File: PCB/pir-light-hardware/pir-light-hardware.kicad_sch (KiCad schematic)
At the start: 3 parts

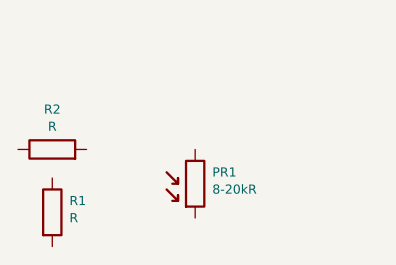
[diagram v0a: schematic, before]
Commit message: chore(kicad): add next part of component libraries
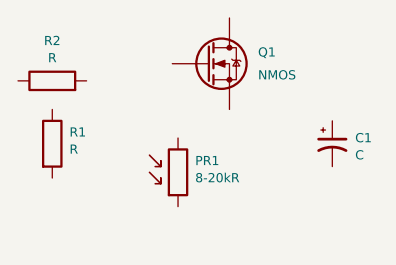
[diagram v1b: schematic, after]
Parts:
- added C1: C, REST:CP_Elec_4x5.4, symbol REST:C_Polarized
- added Q1: NMOS, AON7240:AON7240, symbol AON7240:AON7240
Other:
- moved on the sheet: PR1, R1, R2
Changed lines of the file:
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@@
 	(symbol
 		(lib_id "REST:R")
-		(at 121.285 97.79 270)
+		(at 121.285 90.17 270)
 		(unit 1)
 		(body_style 1)
@@
 		(dnp no)
 		(property "Reference" "R1"
-			(at 123.19 96.52 90)
+			(at 123.19 88.9 90)
 			(show_name no)
 			(do_not_autoplace no)
@@
 		)
 		(property "Value" "R"
-			(at 123.19 98.425 90)
+			(at 123.19 90.805 90)
 			(show_name no)
 			(do_not_autoplace no)
@@
 		)
 		(property "Footprint" ""
-			(at 121.285 96.012 90)
+			(at 121.285 88.392 90)
 			(hide yes)
 			(show_name no)
@@
 		)
 		(property "Datasheet" ""
-			(at 121.285 97.79 0)
+			(at 121.285 90.17 0)
 			(hide yes)
 			(show_name no)
@@
 		)
 		(property "Description" "Resistor"
-			(at 128.905 97.79 0)
+			(at 128.905 90.17 0)
 			(hide yes)
 			(show_name no)
@@
 	(symbol
 		(lib_id "GT36528:GT36528")
-		(at 137.16 94.615 270)
+		(at 135.255 93.345 270)
 		(unit 1)
 		(body_style 1)
@@
 		(dnp no)
 		(property "Reference" "PR1"
-			(at 139.065 93.345 90)
+			(at 137.16 92.075 90)
 			(show_name no)
 			(do_not_autoplace no)
@@
 		)
 		(property "Value" "8-20kR"
-			(at 139.065 95.25 90)
+			(at 137.16 93.98 90)
 			(show_name no)
 			(do_not_autoplace no)
@@
 		)
 		(property "Footprint" "GT36528:GT36528"
-			(at 144.145 94.615 0)
+			(at 142.24 93.345 0)
 			(hide yes)
 			(show_name no)
@@
 		)
 		(property "Datasheet" "https://xonstorage.z8.web.core.windows.net/pdf/jingchuang_gt36528_apr22_xonlink.pdf"
-			(at 146.685 94.615 0)
+			(at 144.78 93.345 0)
 			(hide yes)
 			(show_name no)
@@
 		)
 		(property "Description" ""
-			(at 137.16 94.615 0)
+			(at 135.255 93.345 0)
 			(hide yes)
 			(show_name no)
@@
 	(symbol
 		(lib_id "REST:R")
-		(at 121.285 90.805 0)
+		(at 121.285 83.185 0)
 		(unit 1)
 		(body_style 1)
@@
 		(dnp no)
 		(property "Reference" "R2"
-			(at 121.285 86.36 0)
+			(at 121.285 78.74 0)
 			(show_name no)
 			(do_not_autoplace no)
@@
 		)
 		(property "Value" "R"
-			(at 121.285 88.265 0)
+			(at 121.285 80.645 0)
 			(show_name no)
 			(do_not_autoplace no)
@@
 		)
 		(property "Footprint" ""
-			(at 119.507 90.805 90)
+			(at 119.507 83.185 90)
 			(hide yes)
 			(show_name no)
@@
 		)
 		(property "Datasheet" ""
-			(at 121.285 90.805 0)
+			(at 121.285 83.185 0)
 			(hide yes)
 			(show_name no)
@@
 		)
 		(property "Description" "Resistor"
-			(at 121.285 83.185 0)
+			(at 121.285 75.565 0)
 			(hide yes)
 			(show_name no)
@@
 					(unit 1)
 				)
+			)
+		)
+	)
+	(symbol
+		(lib_id "REST:C_Polarized")
+		(at 152.4 90.17 90)
+		(unit 1)
+		(body_style 1)
+		(exclude_from_sim no)
+		(in_bom yes)
+		(on_board yes)
+		(in_pos_files yes)
+		(dnp no)
+		(property "Reference" "C1"
+			(at 154.94 89.535 90)
+			(show_name no)
+			(do_not_autoplace no)
+			(effects
+				(font
+					(size 1.016 1.016)
+				)
+				(justify right)
+			)
+		)
+		(property "Value" "C"
+			(at 154.94 91.44 90)
+			(show_name no)
+			(do_not_autoplace no)
+			(effects
+				(font
+					(size 1.016 1.016)
+				)
+				(justify right)
+			)
+		)
+		(property "Footprint" "REST:CP_Elec_4x5.4"
+			(at 152.4 90.17 0)
+			(hide yes)
+			(show_name no)
+			(do_not_autoplace no)
+			(effects
+				(font
+					(size 1.27 1.27)
+				)
+			)
+		)
+		(property "Datasheet" ""
+			(at 152.4 90.17 0)
+			(hide yes)
+			(show_name no)
+			(do_not_autoplace no)
+			(effects
+				(font
+					(size 1.27 1.27)
+				)
+			)
+		)
+		(property "Description" "Polarized capacitor, small US symbol"
+			(at 142.875 90.17 0)
+			(hide yes)
+			(show_name no)
+			(do_not_autoplace no)
+			(effects
+				(font
+					(size 1.27 1.27)
+				)
+			)
+		)
+		(pin "1"
+		)
+		(pin "2"
+		)
+		(instances
+			(project "pir-light-hardware"
+				(path "/2adb9c99-9187-4750-a82d-5fddf415ae5e"
+					(reference "C1")
+					(unit 1)
+				)
+			)
+		)
+	)
+	(symbol
+		(lib_id "AON7240:AON7240")
+		(at 139.7 81.28 270)
+		(unit 1)
+		(body_style 1)
+		(exclude_from_sim no)
+		(in_bom yes)
+		(on_board yes)
+		(in_pos_files yes)
+		(dnp no)
+		(fields_autoplaced yes)
+		(property "Reference" "Q1"
+			(at 144.145 80.0099 90)
+			(show_name no)
+			(do_not_autoplace no)
+			(effects
+				(font
+					(size 1.016 1.016)
+				)
+				(justify left)
+			)
+		)
+		(property "Value" "NMOS"
+			(at 144.145 82.5499 90)
+			(show_name no)
+			(do_not_autoplace no)
+			(effects
+				(font
+					(size 1.016 1.016)
+				)
+				(justify left)
+			)
+		)
+		(property "Footprint" "AON7240:AON7240"
+			(at 150.495 81.28 0)
+			(hide yes)
+			(show_name no)
+			(do_not_autoplace no)
+			(effects
+				(font
+					(size 1.27 1.27)
+				)
+			)
+		)
+		(property "Datasheet" "https://www.aosmd.com/sites/default/files/res/datasheets/AON7240.pdf"
+			(at 153.035 81.28 0)
+			(hide yes)
+			(show_name no)
+			(do_not_autoplace no)
+			(effects
+				(font
+					(size 1.27 1.27)
+				)
+			)
+		)
+		(property "Description" ""
+			(at 139.7 81.28 0)
+			(hide yes)
+			(show_name no)
+			(do_not_autoplace no)
+			(effects
+				(font
+					(size 1.27 1.27)
+				)
+			)
+		)
+		(pin "1"
+		)
+		(pin "3"
+		)
+		(pin "2"
+		)
+		(instances
+			(project "pir-light-hardware"
+				(path "/2adb9c99-9187-4750-a82d-5fddf415ae5e"
+					(reference "Q1")
+					(unit 1)
+				)

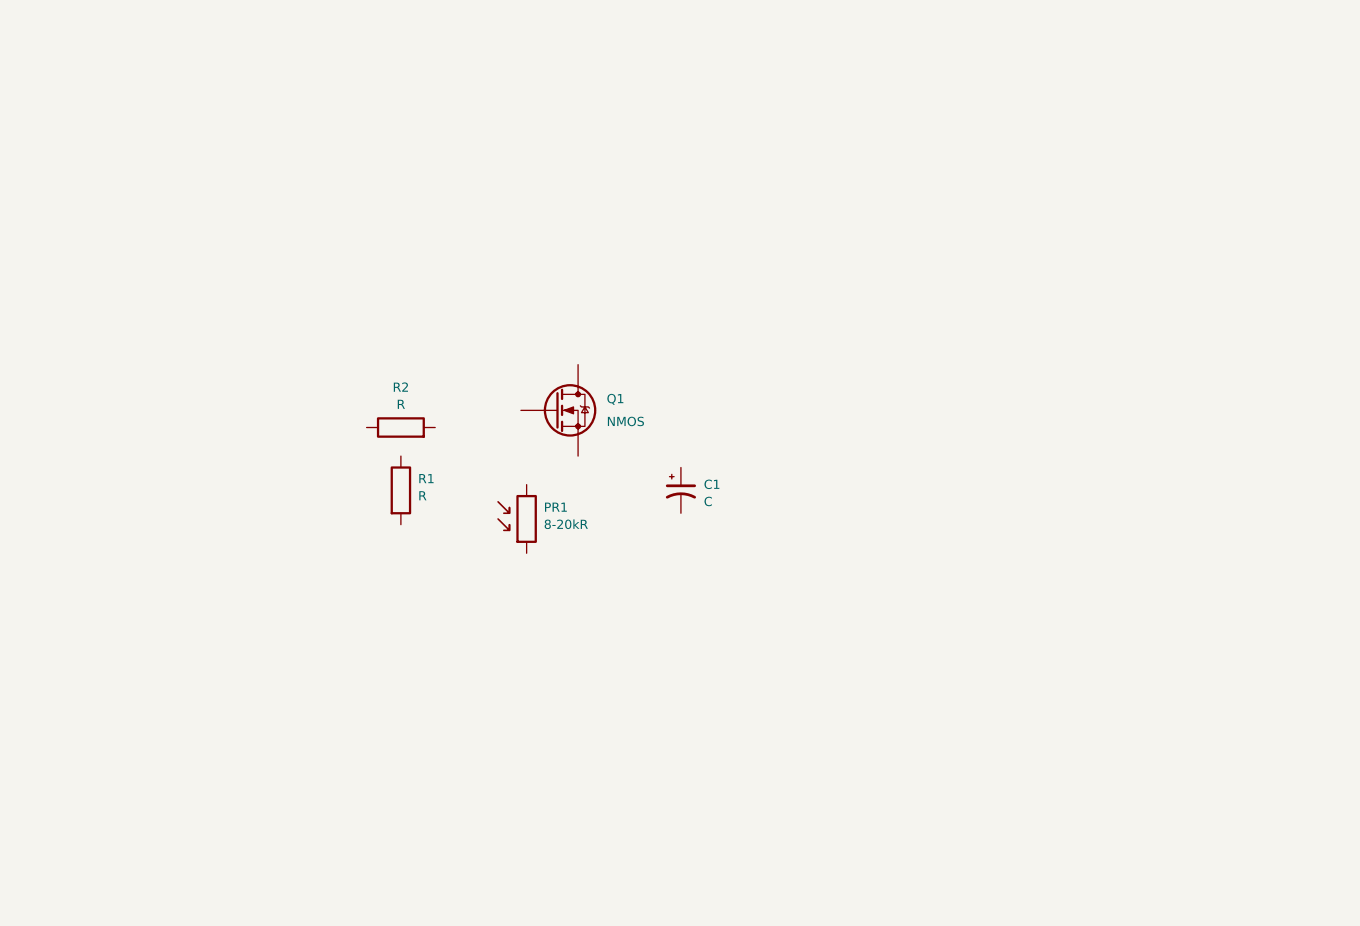
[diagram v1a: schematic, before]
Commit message: chore(kicad): add final part of component libraries
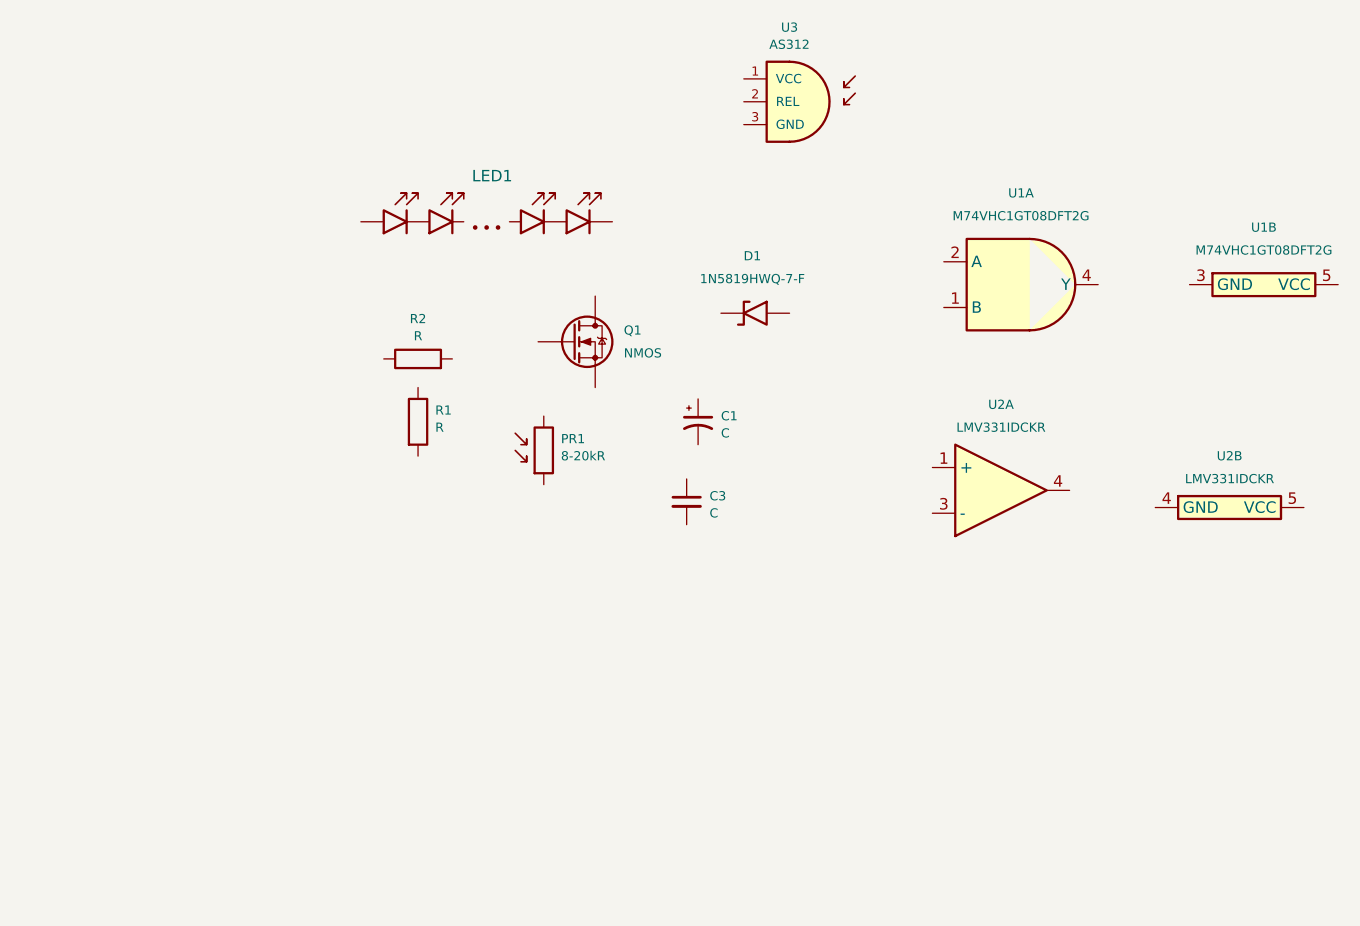
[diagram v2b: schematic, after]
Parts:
- added C3: C, symbol REST:C_MLCC
- added D1: 1N5819HWQ-7-F, 1N5819HWQ-7-F:1N5819HWQ-7-F, symbol 1N5819HWQ-7-F:1N5819HWQ-7-F
- added LED1: (no value), LED-ROD:LED-ROD, symbol LED-ROD:LED-ROD
- added U1: M74VHC1GT08DFT2G, SOT65P210X110-5N, symbol M74VHC1GT08D:M74VHC1GT08DFT2G
- added U2: LMV331IDCKR, SOT65P210X110-5N, symbol LMV331IDCKR:LMV331IDCKR
- added U3: AS312, symbol AS312:AS312
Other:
- moved on the sheet: C1, PR1, Q1, R1, R2

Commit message: chore(kicad): add initial electrical schematic
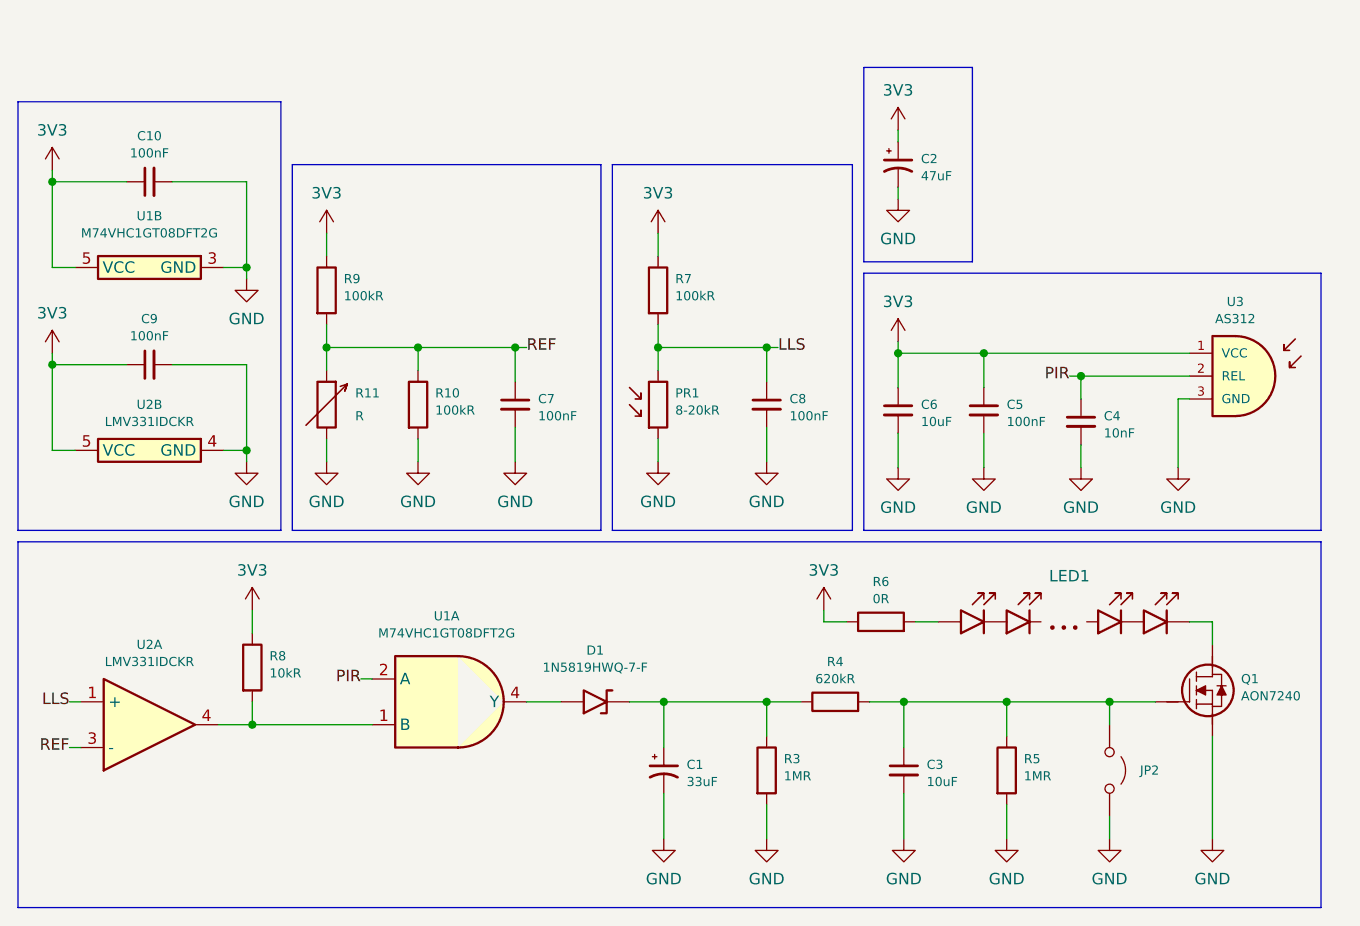
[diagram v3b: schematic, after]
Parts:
- removed R1, R2: R, symbol REST:R
- added C10, C5, C7, C8, C9: 100nF, symbol REST:C_MLCC
- added C2: 47uF, REST:CP_Elec_4x5.4, symbol REST:C_Polarized
- added C4: 10nF, symbol REST:C_MLCC
- added C6: 10uF, symbol REST:C_MLCC
- added JP2: Jumper_Open, symbol REST:Jumper_Open
- added R10, R7, R9: 100kR, symbol REST:R
- added R11: R, symbol REST:R_Variable
- added R3, R5: 1MR, symbol REST:R
- added R4: 620kR, symbol REST:R
- added R6: 0R, symbol REST:R
- added R8: 10kR, symbol REST:R
- C1: value C -> 33uF
- C3: value C -> 10uF
- Q1: value NMOS -> AON7240
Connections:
- net GND: now reaches U2.4 (GND)
- net GND: now also C1.2, C3.2, PR1.2, Q1.1 (S), U1.3 (GND), U3.3 (GND), C10.2, C2.2, C4.2, C5.2, C6.2, C7.2, C8.2, C9.2, JP2.2 (B), R10.2, R11.1, R3.2, R5.2
- net 3V3: now reaches U2.5 (VCC)
- net 3V3: now also U1.5 (VCC), U3.1 (VCC), C10.1, C2.1, C5.1, C6.1, C9.1, R6.1, R7.1, R8.1, R9.1
- net at U1.1 (B): now also U2.4, R8.2
- net PIR: now reaches U1.2 (A)
- net PIR: now also U3.2 (REL), C4.1
- net at U1.4 (Y): now also D1.2 (A)
- net at D1.1 (K): now also C1.1, R3.1, R4.1
- net LLS: now reaches PR1.1
- net LLS: now also U2.1 (+), C8.1, R7.2
- net at LED1.1: now also R6.2
- net at LED1.2: now also Q1.3 (D)
- net REF: now reaches U2.3 (-)
- net REF: now also C7.1, R10.1, R11.2, R9.2
- net at C3.1: now also Q1.2 (G), JP2.1 (A), R4.2, R5.1
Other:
- moved on the sheet: C1, D1, LED1, PR1, U1A, U1B, U2A, U2B, U3
